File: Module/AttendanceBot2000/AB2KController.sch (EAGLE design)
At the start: 59 parts, among them IC1 74AHCT1G04DBV, IC2 74AHCT1G04DBV, IC3 LM386M-1, Q1 2N3904, Q2 2N3904, Q3 2N3904, Q4 2N3904, Q5 2N3904, Q6 2N3904, U1 L298, U2 QRE1113, U3 QRE1113, U4 QRE1113, U5 QRE1113, U6 QRE1113

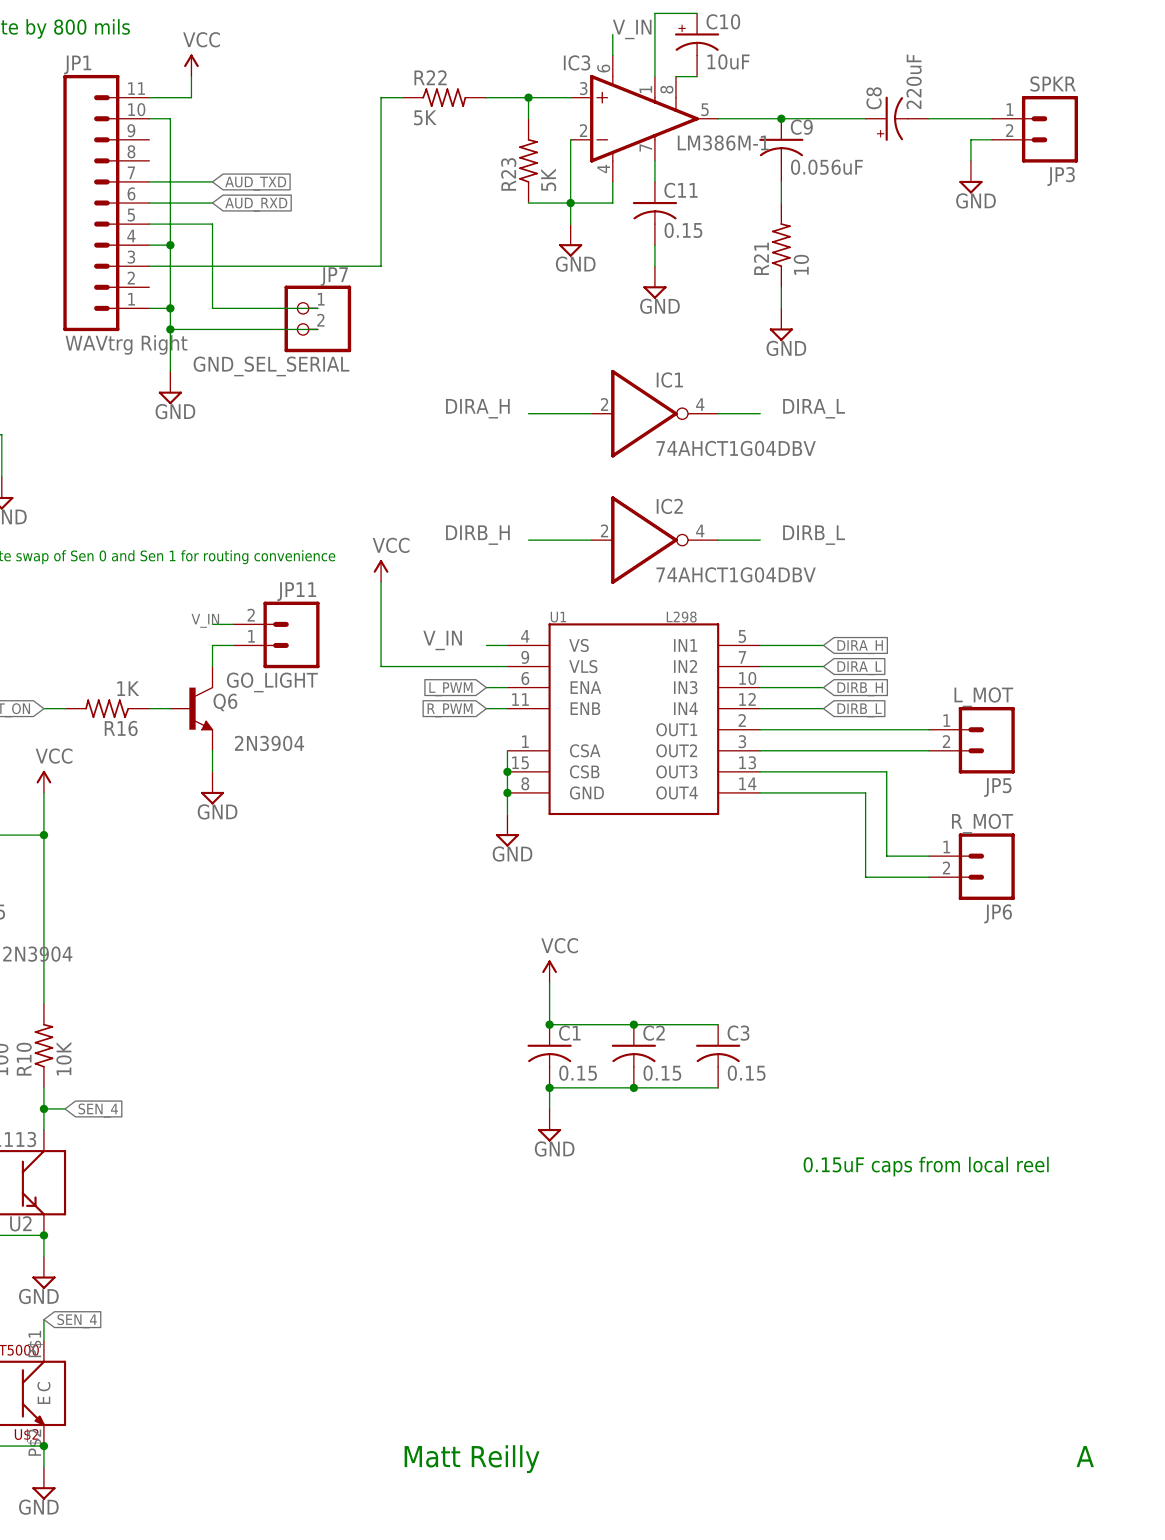
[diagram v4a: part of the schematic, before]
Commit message: Fixed mis-wiring of AUD_TXD and AUD_RXD in sch and board.
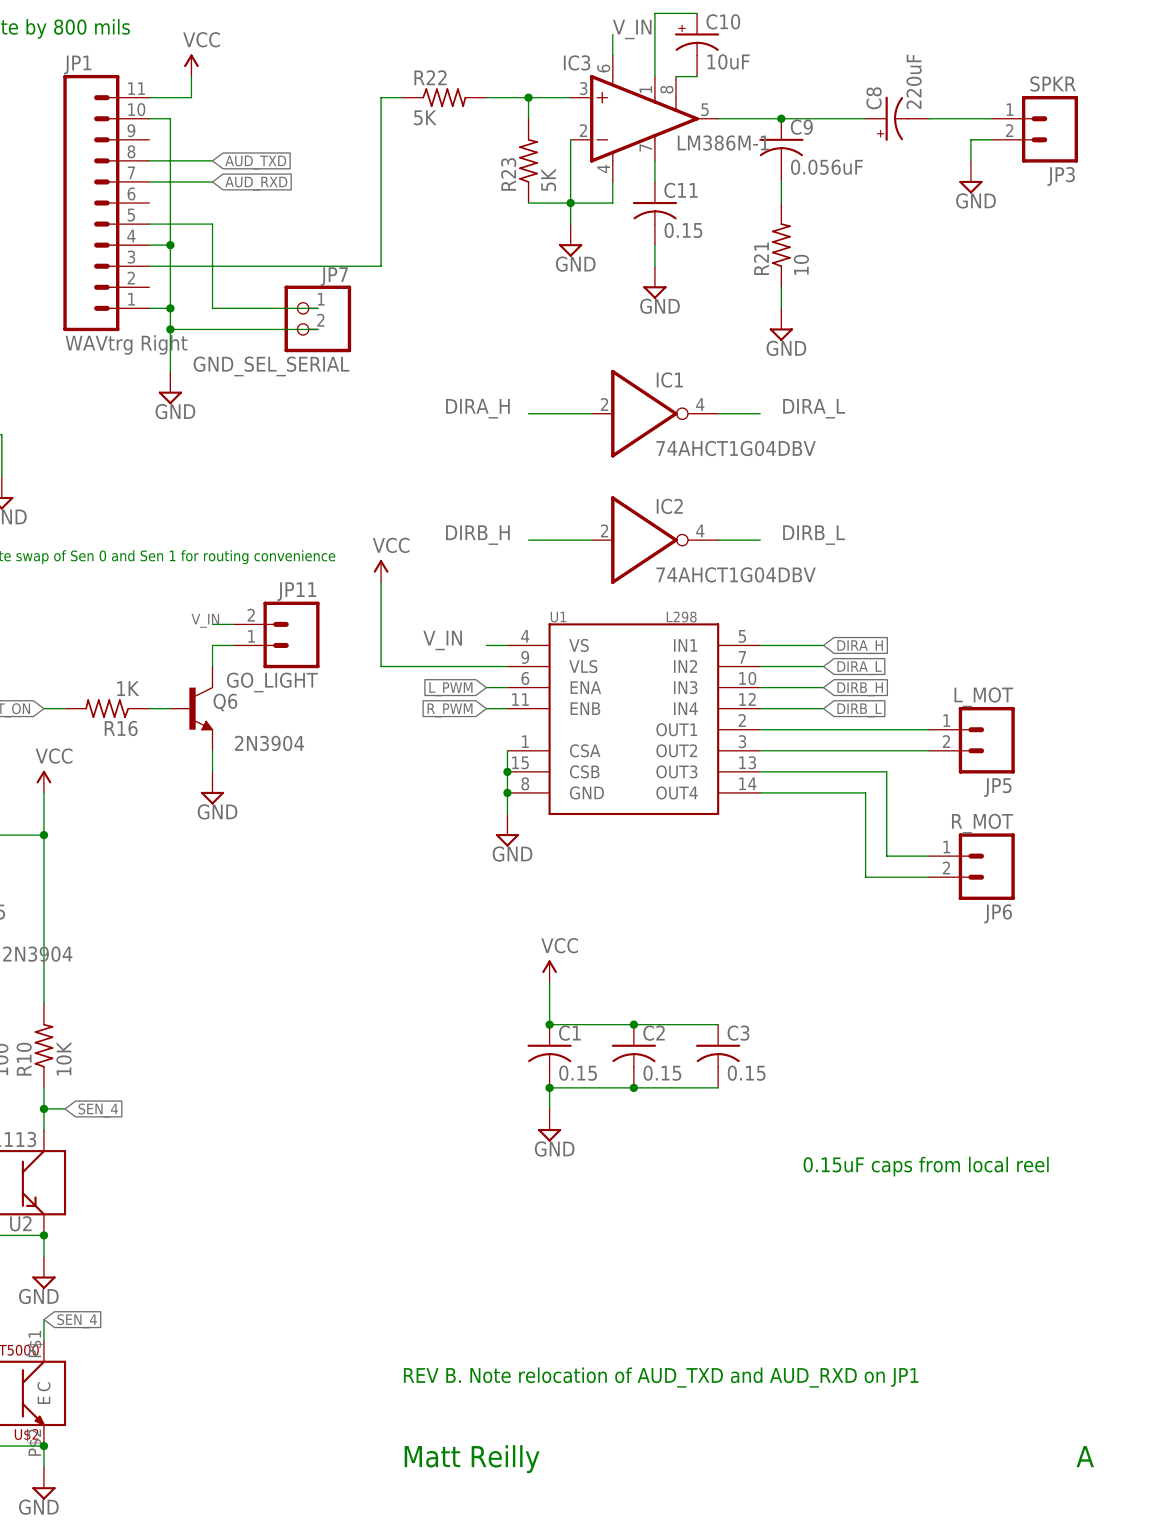
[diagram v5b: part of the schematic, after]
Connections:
- net AUD_RXD: now also JP1.7; no longer JP1.6
- net AUD_TXD: now also JP1.8; no longer JP1.7
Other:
- note added: "REV B. Note relocation of AUD_TXD and AUD_RXD on JP1"
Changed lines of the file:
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@@
 <text x="-12.7" y="38.1" size="2.54" layer="91">A</text>
 <text x="-144.78" y="147.32" size="1.27" layer="91">Note swap of Sen 0 and Sen 1 for routing convenience</text>
+<text x="-93.98" y="48.26" size="1.778" layer="91">REV B. Note relocation of AUD_TXD and AUD_RXD on JP1</text>
 </plain>
 <instances>
@@
 <net name="AUD_TXD" class="0">
 <segment>
-<pinref part="JP1" gate="G$1" pin="7"/>
-<wire x1="-124.46" y1="193.04" x2="-116.84" y2="193.04" width="0.1524" layer="91"/>
-<label x="-116.84" y="193.04" size="1.27" layer="95" xref="yes"/>
+<label x="-116.84" y="195.58" size="1.27" layer="95" xref="yes"/>
+<pinref part="JP1" gate="G$1" pin="8"/>
+<wire x1="-116.84" y1="195.58" x2="-124.46" y2="195.58" width="0.1524" layer="91"/>
 </segment>
 <segment>
@@
 <net name="AUD_RXD" class="0">
 <segment>
-<pinref part="JP1" gate="G$1" pin="6"/>
-<wire x1="-124.46" y1="190.5" x2="-116.84" y2="190.5" width="0.1524" layer="91"/>
-<label x="-116.84" y="190.5" size="1.27" layer="95" xref="yes"/>
-</segment>
-<segment>
+<label x="-116.84" y="193.04" size="1.27" layer="95" xref="yes"/>
+<pinref part="JP1" gate="G$1" pin="7"/>
+<wire x1="-124.46" y1="193.04" x2="-116.84" y2="193.04" width="0.1524" layer="91"/>
+</segment>
+<segment>

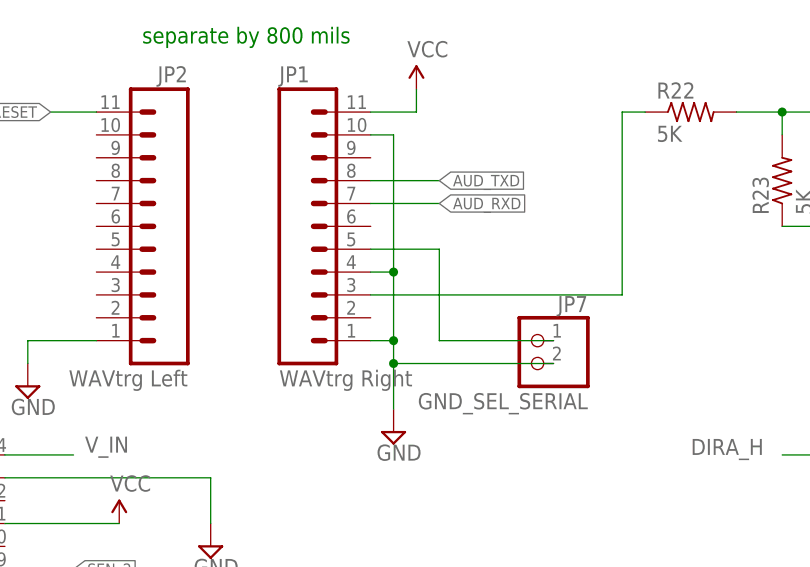
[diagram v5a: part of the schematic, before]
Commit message: Fixed misconnect for UG vs CS...
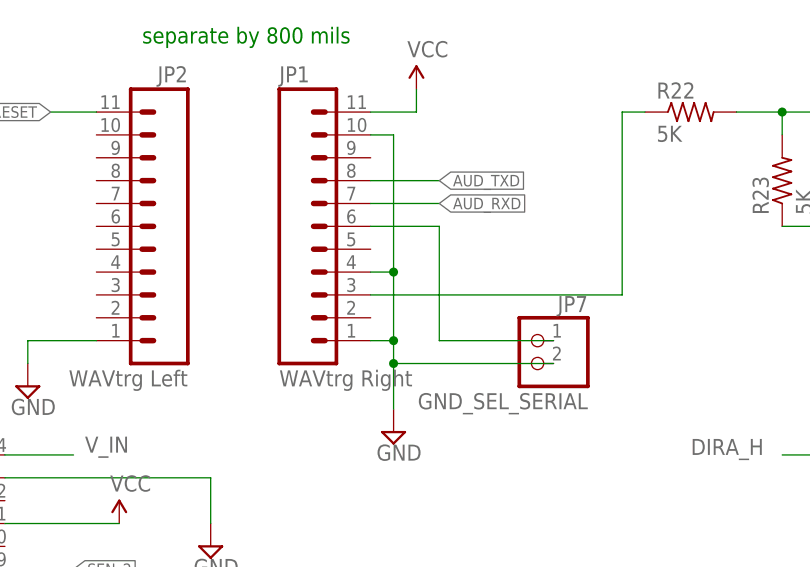
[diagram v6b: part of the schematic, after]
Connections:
- net N$28: now also JP1.6; no longer JP1.5
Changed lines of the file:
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@@
 <net name="N$28" class="0">
 <segment>
-<pinref part="JP1" gate="G$1" pin="5"/>
-<wire x1="-124.46" y1="187.96" x2="-116.84" y2="187.96" width="0.1524" layer="91"/>
-<wire x1="-116.84" y1="187.96" x2="-116.84" y2="177.8" width="0.1524" layer="91"/>
+<wire x1="-116.84" y1="190.5" x2="-116.84" y2="177.8" width="0.1524" layer="91"/>
 <pinref part="JP7" gate="G$1" pin="1"/>
 <wire x1="-116.84" y1="177.8" x2="-104.14" y2="177.8" width="0.1524" layer="91"/>
+<pinref part="JP1" gate="G$1" pin="6"/>
+<wire x1="-124.46" y1="190.5" x2="-116.84" y2="190.5" width="0.1524" layer="91"/>
 </segment>
 </net>

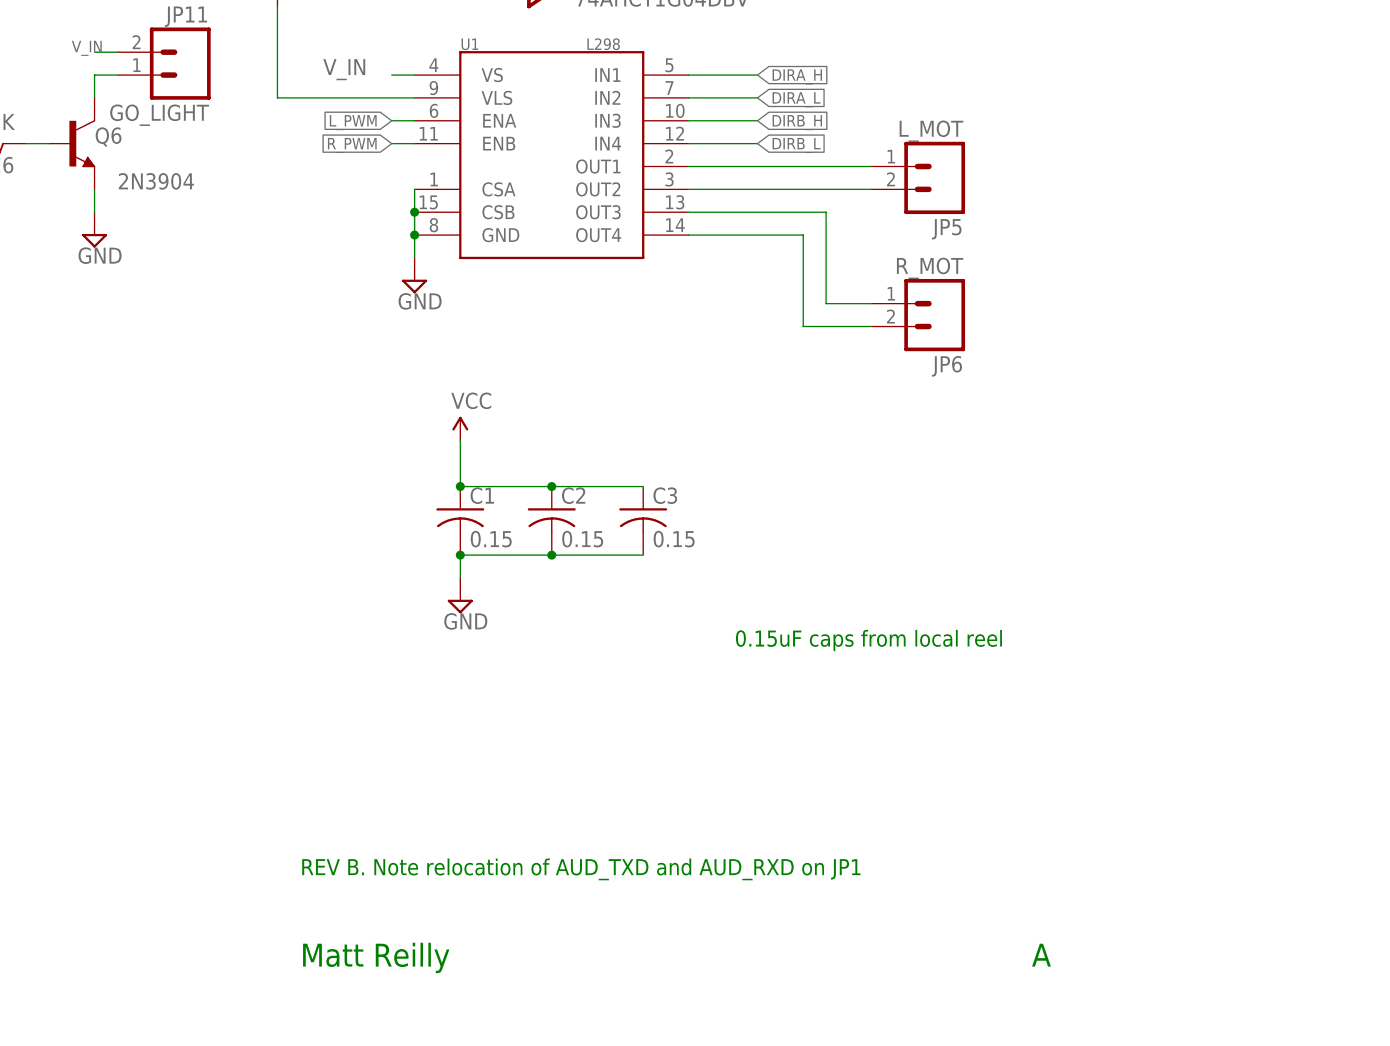
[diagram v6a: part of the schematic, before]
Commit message: Added snubber diodes to motor outputs.
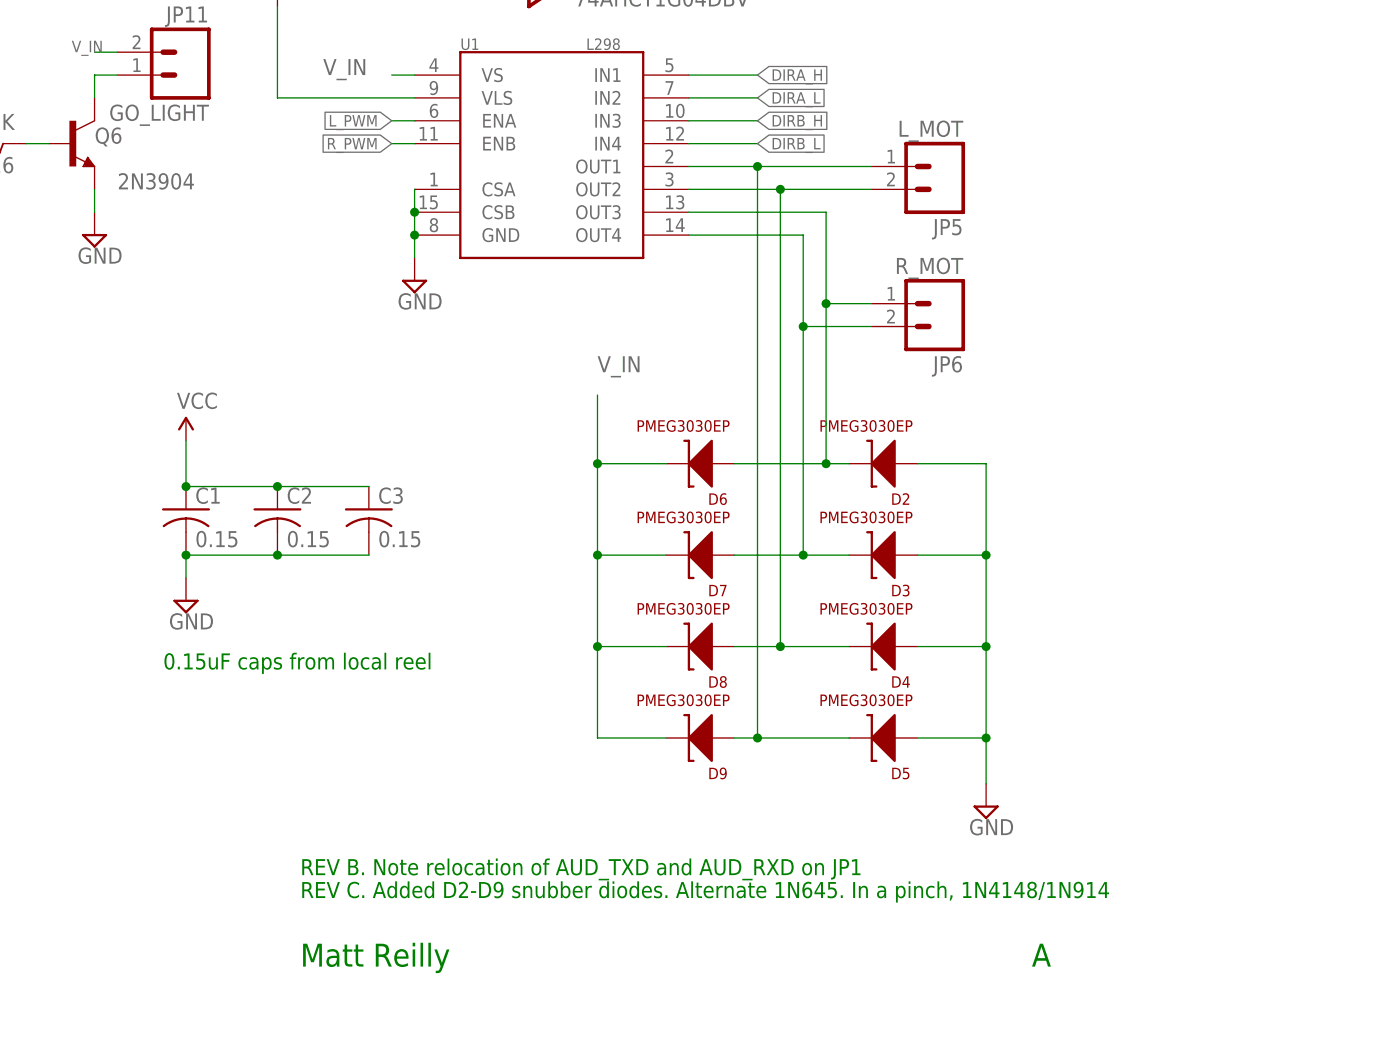
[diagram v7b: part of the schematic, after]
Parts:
- added D2, D3, D4, D5, D6, D7, D8, D9: PMEG3030EP, kb1vc_robot_parts:PMEG3030EP
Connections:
- net GND: now also D2.A, D3.A, D4.A, D5.A
- net N$1: now also D5.C, D9.A
- net N$2: now also D4.C, D8.A
- net N$3: now also D2.C, D6.A
- net N$4: now also D3.C, D7.A
- net V_IN: now also D6.C, D7.C, D8.C, D9.C
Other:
- note added: "REV C. Added D2-D9 snubber diodes. Alternate 1N645. In a pinch, 1N4148/1N914"
- moved on the sheet: C1, C2, C3
